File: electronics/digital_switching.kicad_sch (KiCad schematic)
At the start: 16 parts, among them J5 DB12, U10 BTS7006, U6 BTS7006, U7 BTS7006, U8 BTS7006, U9 BTS7006

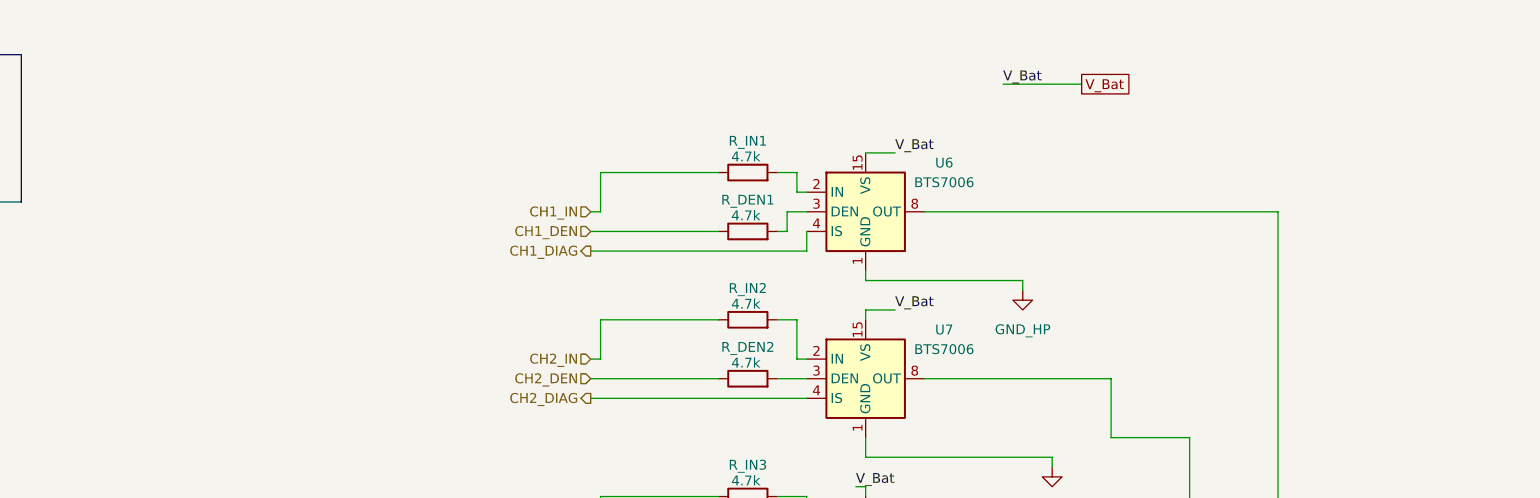
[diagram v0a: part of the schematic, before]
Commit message: add some more part nummbers
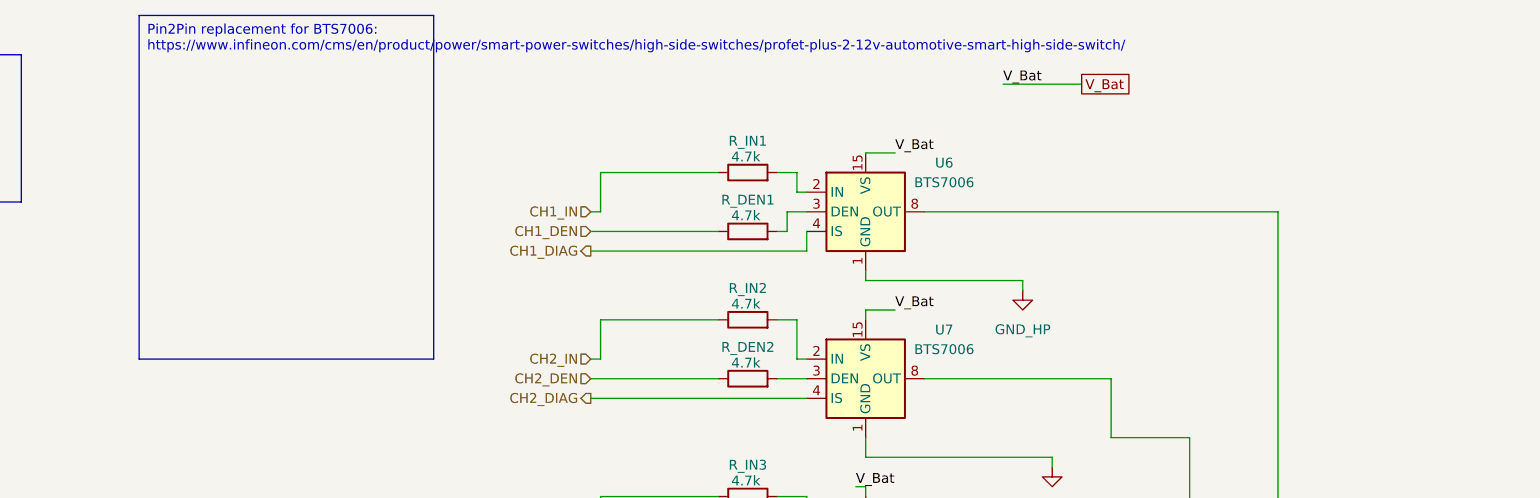
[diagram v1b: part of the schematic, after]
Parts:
- J5: LCSCc (none) -> C2927513
- U6: Mouser (none) -> 726-BTS70061EPPXUMA1
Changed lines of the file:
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@@
+		)
+	)
+	(text_box "Pin2Pin replacement for BTS7006:\nhttps://www.infineon.com/cms/en/product/power/smart-power-switches/high-side-switches/profet-plus-2-12v-automotive-smart-high-side-switch/\n"
+		(exclude_from_sim no)
+		(at 111.76 16.51 0)
+		(size 38.1 44.45)
+		(stroke
+			(width 0)
+			(type default)
+		)
+		(fill
+			(type none)
+		)
+		(effects
+			(font
+				(size 1.27 1.27)
+			)
+			(justify left top)
 		)
 	)
@@
 		(property "Description" "Smart High-Side Power Switch, PROFET, One Channel, 12V, 15A, Rds(on) 4.4mΩ, PG-TSDSO-14-22"
 			(at 201.676 64.77 0)
+			(effects
+				(font
+					(size 1.27 1.27)
+				)
+				(hide yes)
+			)
+		)
+		(property "TME" ""
+			(at 205.74 41.91 0)
+			(effects
+				(font
+					(size 1.27 1.27)
+				)
+				(hide yes)
+			)
+		)
+		(property "Mouser" "726-BTS70061EPPXUMA1"
+			(at 205.74 41.91 0)
+			(effects
+				(font
+					(size 1.27 1.27)
+				)
+				(hide yes)
+			)
+		)
+		(property "LCSC" ""
+			(at 205.74 41.91 0)
 			(effects
 				(font
@@
 			(at 267.97 90.17 0)
 			(effects
+				(font
+					(size 1.27 1.27)
+				)
+				(hide yes)
+			)
+		)
+		(property "LCSCc" "C2927513"
+			(at 267.97 90.17 0)
+			(effects
+				(font
+					(size 1.27 1.27)
+				)
+				(hide yes)
+			)
+		)
+		(property "TME" ""
+			(at 267.97 90.17 0)
+			(effects
